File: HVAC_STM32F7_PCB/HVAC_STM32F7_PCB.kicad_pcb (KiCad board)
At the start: 4 copper layers, 197.3 x 123 mm, 98 parts, among them J1 DC_Jack_5.5x2.1mm, J10 OUT_Signal_connector, J11 OUT_Signal_connector, J12 OUT_Signal_connector, J13 OUT_Signal_connector, J14 Signal_connector, J15 Signal_connector, J16 Signal_connector, J17 Signal_connector, J2 Signal_connector, J3 Signal_connector, J4 Signal_connector, J5 Signal_connector, J6 OUT_Signal_connector, J7 OUT_Signal_connector, J8 OUT_Signal_connector, J9 OUT_Signal_connector, Q1 IRLML9301, SW1 SLW-1276864-4A-D, U1 LM2596S-5, U2 LM2596S-3.3, U3 DAC7568IAPW, U5 TLV9304xPW, U6 TLV9304xPW, U7 ADS8688

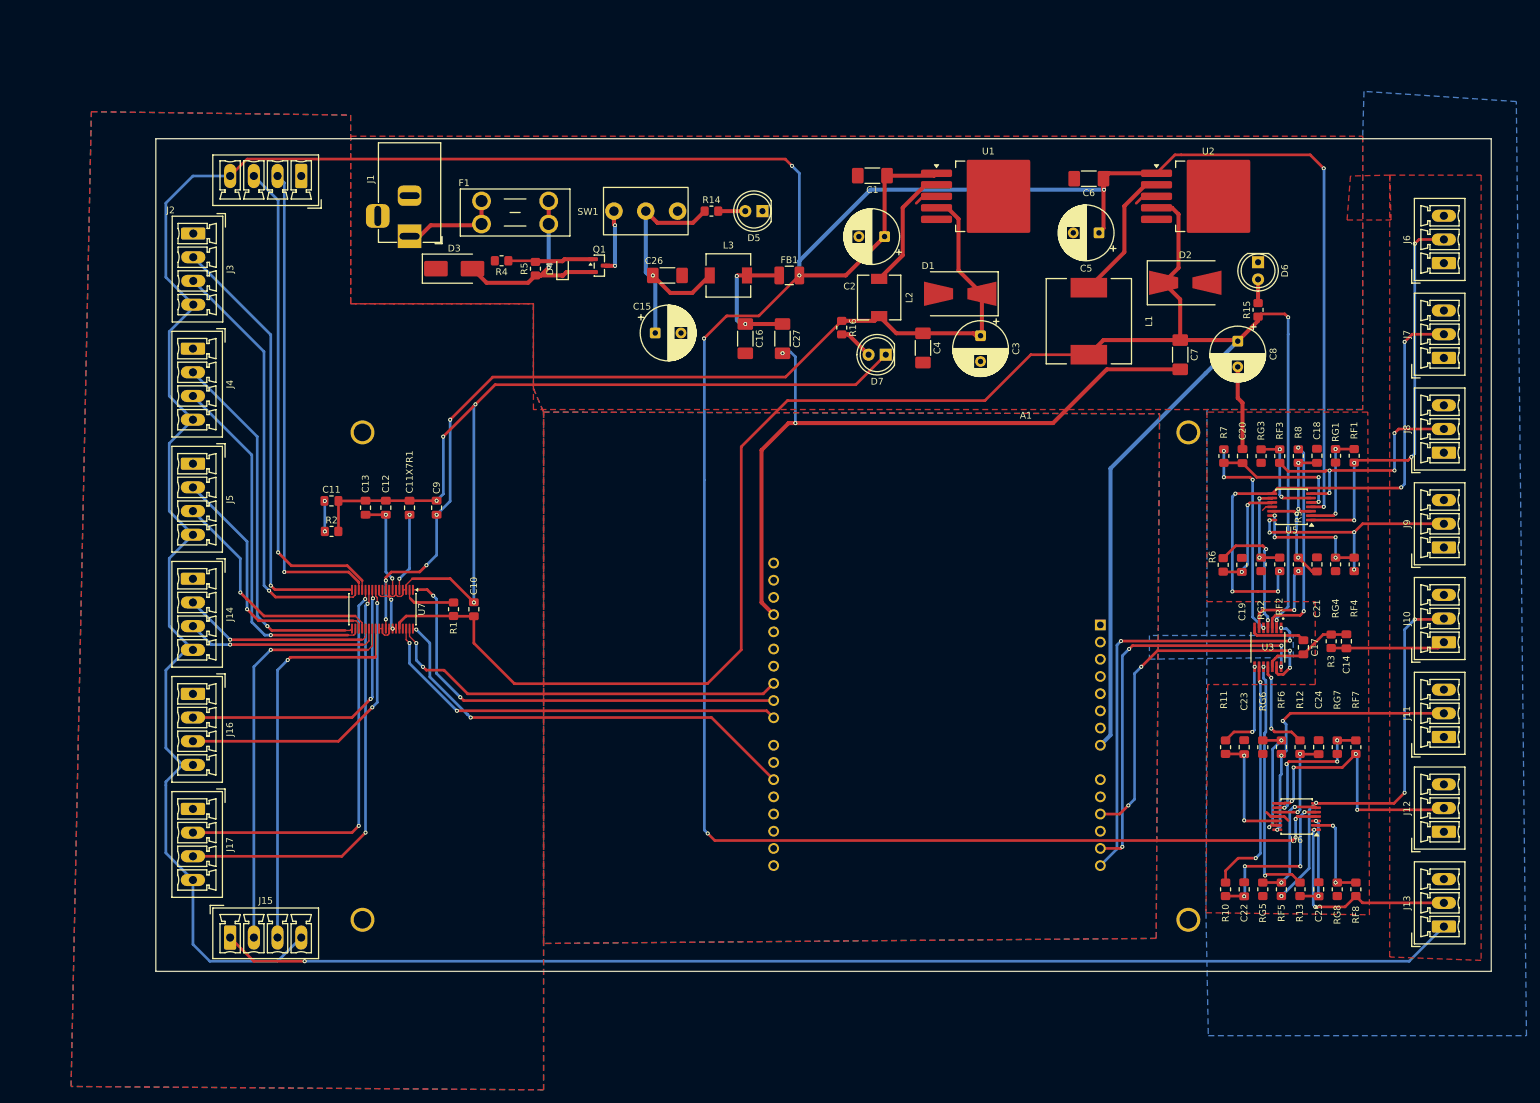
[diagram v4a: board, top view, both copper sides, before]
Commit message: ADD kosmetyka większości opisów komponenów, TODO: ogarnąć masę zasilania aktywnych czujników
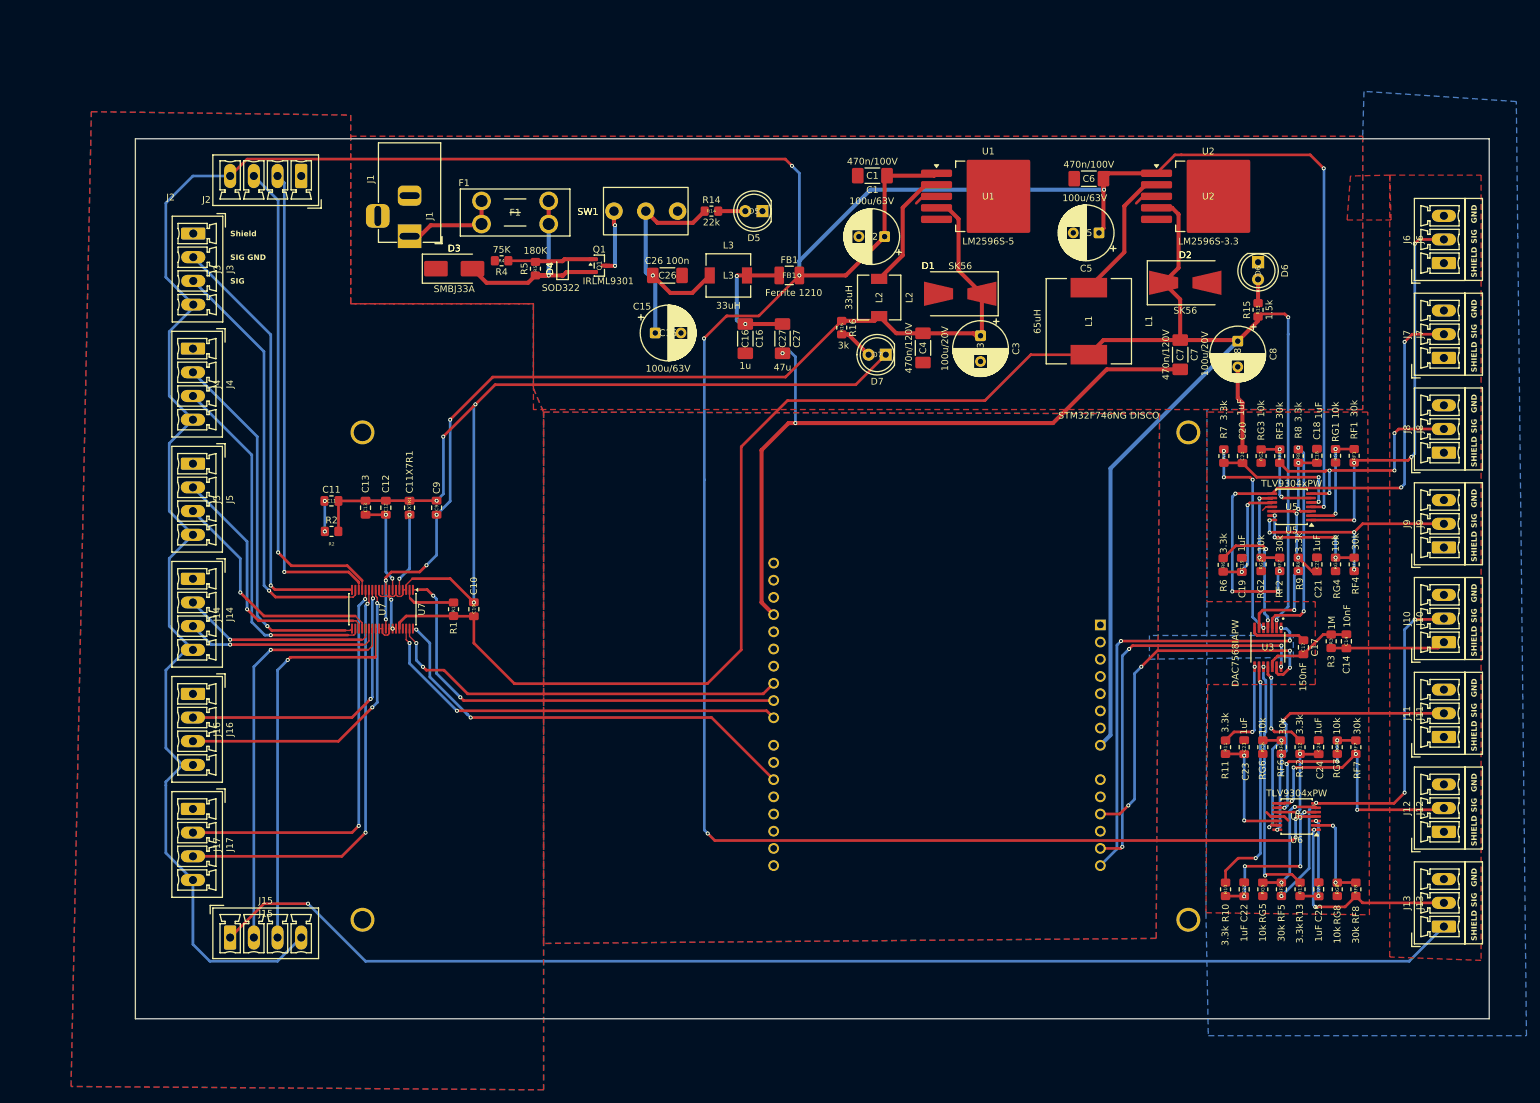
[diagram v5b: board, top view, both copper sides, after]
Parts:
- FB1: value Ferrite Bead 1210 -> Ferrite 1210
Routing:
- net GNDA: track 204.4 -> 208.6 mm
- net Net-(D3-A2): track 31.7 -> 32.4 mm
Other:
- board size 197.3 x 123 mm -> 200 x 130 mm
- board text added: "GND"
- board text added: "SHIELD"
- board text added: "SIG"
- board text added: "SIG GND"
- board text added: "Shield"

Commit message: ADD Poprawki PCB layout TODO zasilanie toru wyjciowego, podpisy elementow i kosmetyka
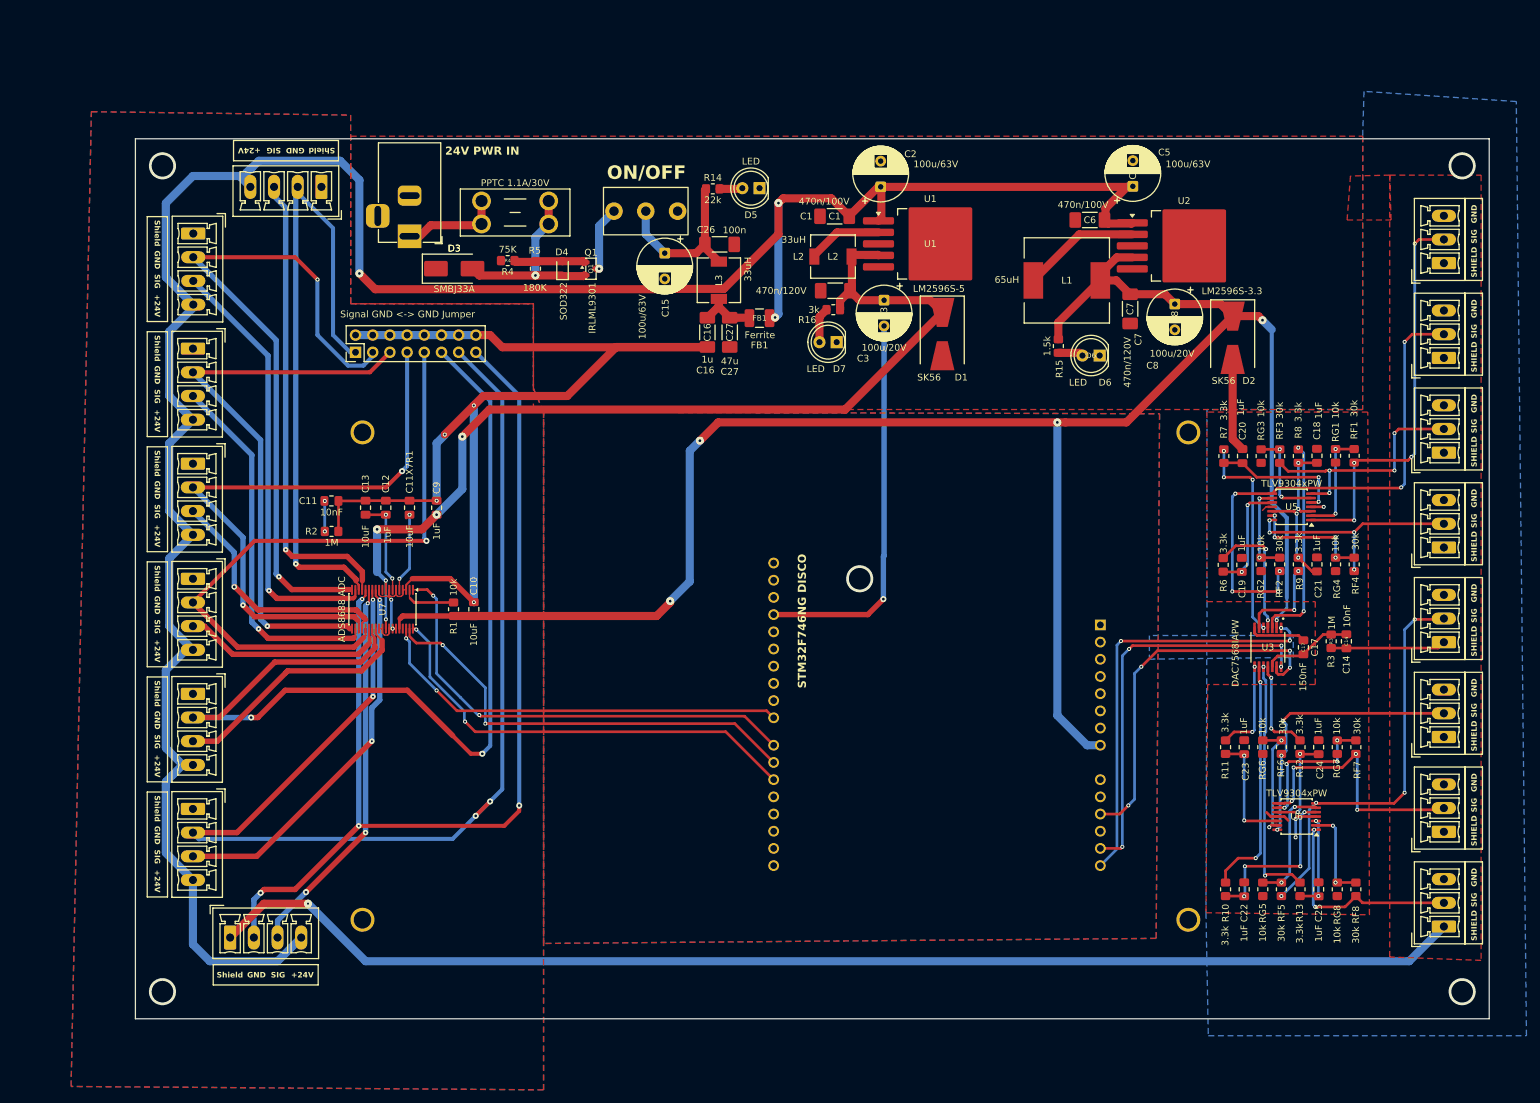
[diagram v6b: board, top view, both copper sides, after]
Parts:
- added J18: Conn_02x08_Odd_Even, Connector_PinHeader_2.54mm:PinHeader_2x08_P2.54mm_Vertical, F.Cu at (63.5, 62.5)
- FB1: value Ferrite 1210 -> Ferrite
- SW1: value SLW-1276864-4A-D -> ON/OFF
- U7: value ADS8688 -> ADS8688 ADC
- moved R15 30.0 mm to (167.3, 61.6), turned to -90 degrees
- moved D6 27.2 mm to (173.4, 63.0), turned to 180 degrees
- moved C4 15.5 mm to (134.4, 53.5), turned to 180 degrees
- moved C3 15.2 mm to (141.6, 54.8)
- moved C15 11.9 mm to (109.2, 47.9), turned to -90 degrees
- moved U1 11.1 mm to (148.4, 46.5)
- moved C8 10.8 mm to (184.6, 55.4)
- moved D2 10.7 mm to (193.1, 60.4), turned to -90 degrees
- moved C7 10.0 mm to (177.9, 56.1)
- moved L2 9.12 mm to (134.1, 48.4), turned to 0 degrees
- moved C26 8.96 mm to (117.3, 46.6)
- moved C5 8.50 mm to (178.3, 38.0), turned to 90 degrees
- moved C1 8.19 mm to (134.3, 42.5)
- moved U2 8.15 mm to (185.9, 46.8)
- moved C27 7.85 mm to (118.8, 59.6)
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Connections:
- A1 pad 21: unconnected-(A1-D6-Pad21) -> Net-(A1-D6)
- A1 pad 22: unconnected-(A1-D7-Pad22) -> Net-(A1-D7)
- A1 pad 24: Net-(A1-D9) -> unconnected-(A1-D9-Pad24)
- A1 pad 25: Net-(A1-D10) -> unconnected-(A1-D10-Pad25)
- U5 pad 4: +24V -> unconnected-(U5E-V+-Pad4)
- U6 pad 4: +24V -> unconnected-(U6E-V+-Pad4)
- U7 pad 1: Net-(A1-D9) -> Net-(A1-D7)
- U7 pad 12: Net-(J16-SIG) -> Net-(J17-SIG)
- U7 pad 13: Net-(J16-GND) -> Net-(J17-GND)
- U7 pad 14: Net-(J17-SIG) -> Net-(J15-SIG)
- U7 pad 15: Net-(J17-GND) -> Net-(J15-GND)
- U7 pad 26: Net-(J15-GND) -> Net-(J16-GND)
- U7 pad 27: Net-(J15-SIG) -> Net-(J16-SIG)
- U7 pad 37: Net-(A1-D10) -> Net-(A1-D6)
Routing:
- net +24V: track 622.7 -> 355.7 mm, vias 9 -> 3
- net Net-(J17-GND): track 60.2 -> 170.0 mm, vias 2 -> 4
- net Net-(J16-GND): track 43.7 -> 145.3 mm
- net Net-(J15-GND): track 61.3 -> 155.9 mm, vias 1 -> 4
- net Net-(A1-D7): track 0.00 -> 69.3 mm, vias 0 -> 2
- net Net-(J14-GND): track 29.2 -> 96.2 mm
- net Net-(A1-D9): track 66.5 -> 0.00 mm, vias 2 -> 0
- net Net-(A1-D6): track 0.00 -> 65.8 mm, vias 0 -> 2
- net Net-(A1-D10): track 60.6 -> 0.00 mm, vias 2 -> 0
- net Net-(J18-Pin_7): track 39.4 -> 89.4 mm, vias 1 -> 2
- net Net-(J18-Pin_3): track 65.5 -> 102.8 mm, vias 1 -> 2
- net Net-(J18-Pin_5): track 54.9 -> 84.7 mm
- net GND: track 303.1 -> 275.9 mm, vias 8 -> 7
- net Net-(J18-Pin_1): track 71.7 -> 95.8 mm
- net +3.3V: track 319.5 -> 298.4 mm, vias 2 -> 5
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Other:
- board text added: "+24V"
- board text added: "24V PWR IN"
- board text added: "Signal GND <-> GND Jumper"
- board text removed: "SIG GND"

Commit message: ADD final pcb version for review, god bless
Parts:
- added C28: 100n, Capacitor_SMD:C_0805_2012Metric_Pad1.18x1.45mm_HandSolder, F.Cu at (199.0, 36.5)
- added C29: 4.7u/50V, Capacitor_SMD:C_2220_5750Metric_Pad1.97x5.40mm_HandSolder, F.Cu at (200.8, 42.2)
- added C30: 10u, Capacitor_SMD:C_0805_2012Metric_Pad1.18x1.45mm_HandSolder, F.Cu at (203.5, 50.5)
- added C31: 100n/50V, Capacitor_SMD:C_0805_2012Metric_Pad1.18x1.45mm_HandSolder, F.Cu at (203.8, 54.0)
- added C32: 100n, Capacitor_SMD:C_0805_2012Metric_Pad1.18x1.45mm_HandSolder, F.Cu at (208.2, 84.8)
- added C33: 100n, Capacitor_SMD:C_0805_2012Metric_Pad1.18x1.45mm_HandSolder, F.Cu at (208.8, 130.8)
- added F2: Fuse, Fuse:Fuse_1812_4532Metric_Pad1.30x3.40mm_HandSolder, F.Cu at (193.0, 37.5)
- added R17: 10k, Resistor_SMD:R_0805_2012Metric_Pad1.20x1.40mm_HandSolder, F.Cu at (198.8, 49.5)
- U7: value ADS8688 ADC -> ADS8688
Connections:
- U5 pad 4: unconnected-(U5E-V+-Pad4) -> Net-(U5E-V+)
- U6 pad 4: unconnected-(U6E-V+-Pad4) -> Net-(U5E-V+)
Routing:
- net Net-(U5E-V+): track 0.00 -> 155.3 mm, vias 0 -> 5
- net Net-(C28-Pad1): track 0.00 -> 14.9 mm
- net GND: track 275.9 -> 290.3 mm, vias 7 -> 11
- net +24V: track 355.7 -> 368.4 mm
- net unconnected-(U6E-V+-Pad4): track 5.94 -> 0.00 mm, vias 2 -> 0
- net unconnected-(U5E-V+-Pad4): track 1.96 -> 0.00 mm, vias 1 -> 0
- net Net-(J12-GND): track 38.7 -> 37.9 mm
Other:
- board text added: "IN CH1"
- board text added: "IN CH2"
- board text added: "IN CH3"
- board text added: "IN CH4"
- board text added: "IN CH5"
- board text added: "IN CH6"
- board text added: "IN CH7"
- board text added: "IN CH8"
- board text added: "OUT CH1"
- board text added: "OUT CH2"
- board text added: "OUT CH3"
- board text added: "OUT CH4"
- board text added: "OUT CH5"
- board text added: "OUT CH6"
- board text added: "OUT CH7"
- board text added: "OUT CH8"
- board text added: "Projekt Dyplomowy Inżynierski Paweł Bałbatun 2025"

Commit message: ADD hopefully finished pcb project
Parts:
- removed R5: 180K, Resistor_SMD:R_0805_2012Metric_Pad1.20x1.40mm_HandSolder
- D4: value SOD322 -> 1N4742A; footprint Diode_SMD:D_SOD-323F -> Diode_THT:D_DO-41_SOD81_P2.54mm_Vertical_AnodeUp
- Q1: value IRLML9301 -> AO4407A; footprint Package_TO_SOT_SMD:SOT-23 -> własne:PowerPAK_SO-8_Single
- moved D4 2.31 mm to (93.5, 48.0), turned to -90 degrees
- moved Q1 2.30 mm to (100.2, 48.9)
- moved C5 0.58 mm to (178.3, 38.6)
- turned L1 to -90 degrees
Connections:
- D4 pad 1: Net-(D3-A2) -> Net-(D4-K)
- Q1 pad 2: Net-(D3-A2) -> Net-(D4-K)
- Q1 pad 3: Net-(Q1-D) -> Net-(D3-A2)
- SW1 pad 1: Net-(Q1-D) -> Net-(D4-K)
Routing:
- net Net-(D4-K): track 0.00 -> 15.4 mm
- net Net-(Q1-D): track 9.90 -> 0.00 mm, vias 1 -> 0
- net Net-(U2-OUT): track 17.4 -> 10.4 mm
- net +3.3V: track 298.4 -> 304.7 mm
- net Net-(J17-SIG): track 56.6 -> 62.3 mm
- net +24V: track 368.4 -> 372.4 mm
- net Net-(D3-A2): track 28.8 -> 32.8 mm, vias 1 -> 2
- net Net-(J15-SIG): track 57.0 -> 60.7 mm
- net GND: track 290.3 -> 293.6 mm, vias 11 -> 159
- net Net-(J14-SIG): track 30.4 -> 32.7 mm
- net Net-(J17-GND): track 170.0 -> 172.2 mm
- net Net-(J18-Pin_3): track 102.8 -> 100.8 mm
- net Net-(J18-Pin_1): track 95.8 -> 93.9 mm
- net Net-(J3-SIG): track 64.7 -> 62.8 mm
- net Net-(J2-SIG): track 69.7 -> 68.4 mm
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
